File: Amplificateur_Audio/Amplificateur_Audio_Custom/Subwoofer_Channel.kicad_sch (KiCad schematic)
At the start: 52 parts, among them J901 I2S-OUT, J902 RCJ-024, U901 PCM5252RHBR, U902 NE5532

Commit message: Assignation des composants et empreintes terminé
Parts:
- removed C920: 22pF, symbol Device:C_Small
- removed C921, C923: 10uF, symbol Device:C_Small
- removed JP905: DIN2-SEL, symbol Jumper:Jumper_3_Open
- added C915: 10uF, Capacitor_SMD:C_1206_3216Metric_Pad1.33x1.80mm_HandSolder, symbol Device:C_Small
- added C918: 10uF, Capacitor_SMD:C_0603_1608Metric_Pad1.08x0.95mm_HandSolder, symbol Device:C_Small
- added C919: 22pF, Capacitor_SMD:C_0603_1608Metric_Pad1.08x0.95mm_HandSolder, symbol Device:C_Small
- added JP901: DIN2-SEL, Connector_PinHeader_2.54mm:PinHeader_1x03_P2.54mm_Vertical_SMD_Pin1Left, symbol Jumper:Jumper_3_Open
- C901, C902, C905, C910, C912, C914, C917, C922, C924: footprint (none) -> Capacitor_SMD:C_0603_1608Metric_Pad1.08x0.95mm_HandSolder
- C903, C904, C906, C907, C908, C909, C911: footprint (none) -> Capacitor_SMD:C_0402_1005Metric_Pad0.74x0.62mm_HandSolder
- C913: footprint (none) -> Capacitor_SMD:C_1206_3216Metric_Pad1.33x1.80mm_HandSolder
- C916, C925: footprint (none) -> Capacitor_SMD:C_0805_2012Metric_Pad1.18x1.45mm_HandSolder
- J901: footprint (none) -> Connector_IDC:IDC-Header_2x10_P2.54mm_Vertical_SMD
- J902: footprint (none) -> NewLibrary:CUI_RCJ-024
- L901: footprint (none) -> Inductor_SMD:L_APV_ANR4012
- R901, R909, R910, R911, R912, R915: footprint (none) -> Resistor_SMD:R_0603_1608Metric_Pad0.98x0.95mm_HandSolder
- R902, R903, R904, R905, R908, R913, R914, R916, R917, R918, R919, R920, R921, R922: footprint (none) -> Resistor_SMD:R_0402_1005Metric_Pad0.72x0.64mm_HandSolder
- R906: footprint (none) -> Resistor_SMD:R_0402_1005Metric_Pad0.72x0.64mm_HandSolder; now not fitted
- R907: footprint (none) -> Resistor_SMD:R_0402_1005Metric_Pad0.72x0.64mm_HandSolder; now fitted
- U901: footprint (none) -> Package_DFN_QFN:Texas_RHB0032E_VQFN-32-1EP_5x5mm_P0.5mm_EP3.45x3.45mm_ThermalVias
- U902: footprint (none) -> Package_SO:Texas_HTSOP-8-1EP_3.9x4.9mm_P1.27mm_EP2.95x4.9mm_Mask2.4x3.1mm_ThermalVias
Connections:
- net 12V-OA: now also C916.2, R921.2; no longer R922.1
- net 3V3: now also R906.2, R908.2; no longer R906.1, R907.2
- net DIN2: now also JP901.2 (C)
- net GND: now also C908.1, C916.1, R907.1, R922.1, C918.2; no longer C908.2, R908.1, R921.2
- net at C922.1, R921.1, R922.2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: now also R920.1, C918.1, C919.1; no longer R920.2
- net at C917.2, R915.2, U902.1: now also R917.1; no longer R919.1
- net at J901.11 (Pin_11): now also JP901.1 (A)
- net at J901.13 (Pin_13): now also JP901.3 (B)
- net at C917.1, U902.2 (-): now also R917.2, R918.1; no longer R917.1, R919.2
- net at C913.2: now also R918.2; no longer R917.2
- net at C912.1, R910.1, R914.1: now also C915.1; no longer C916.1
- net at U901.2 (LDOO): now also C908.2; no longer C908.1
- net at U901.1 (XSMT): now also R908.1; no longer R906.2
- new net: C915.2, R919.2
- new net: R906.1, R907.2, U901.22 (GPIO2/ADR2/GPO)
- new net: C919.2, R919.1, R920.2, U902.3 (+)

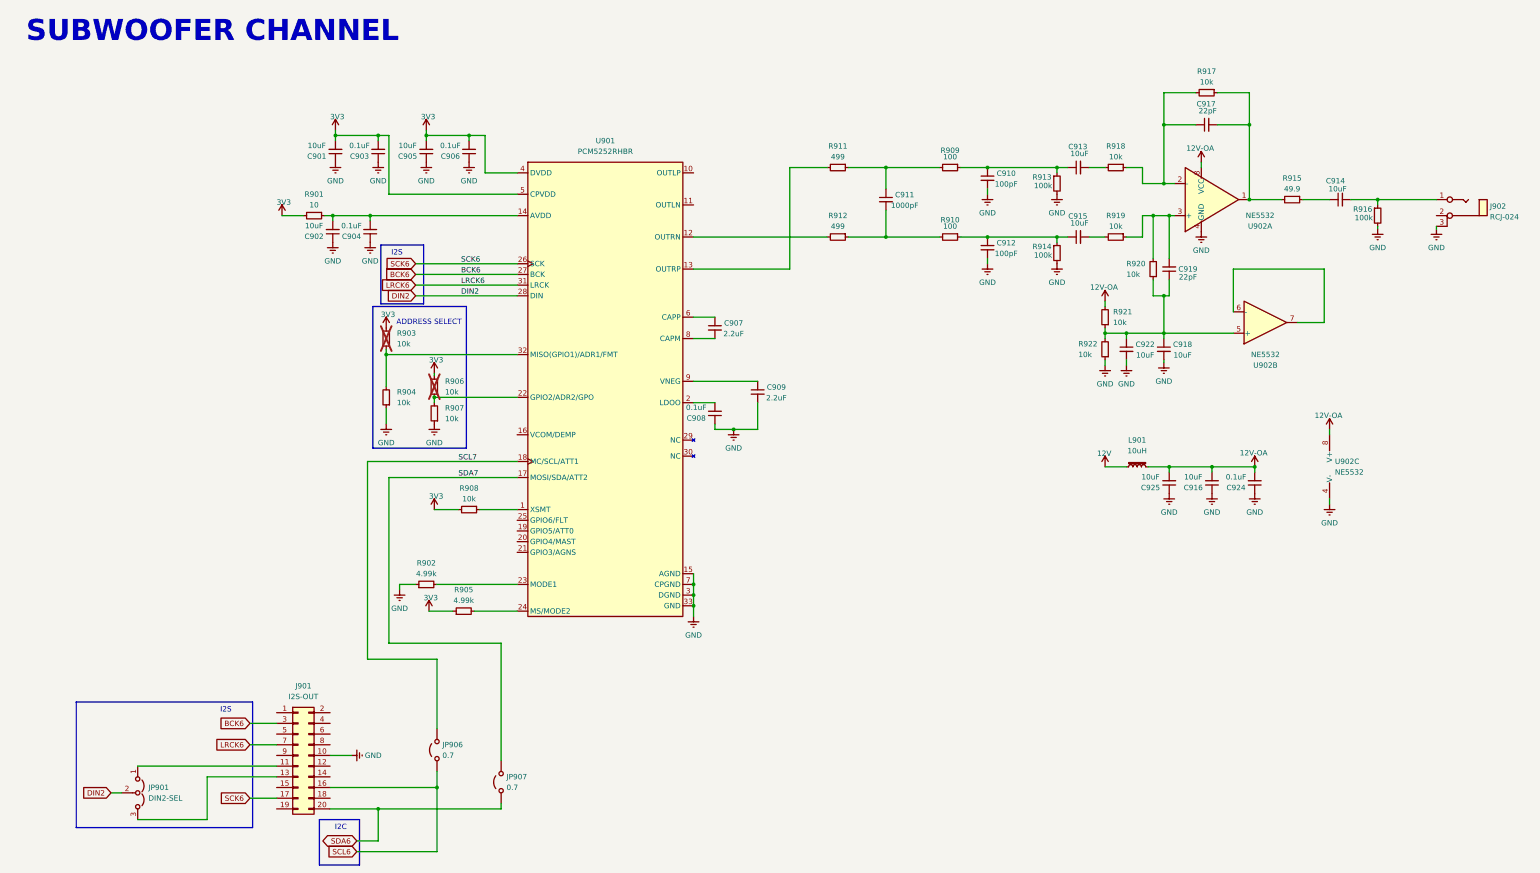
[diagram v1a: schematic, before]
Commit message: Ajout de point de test et début du routage
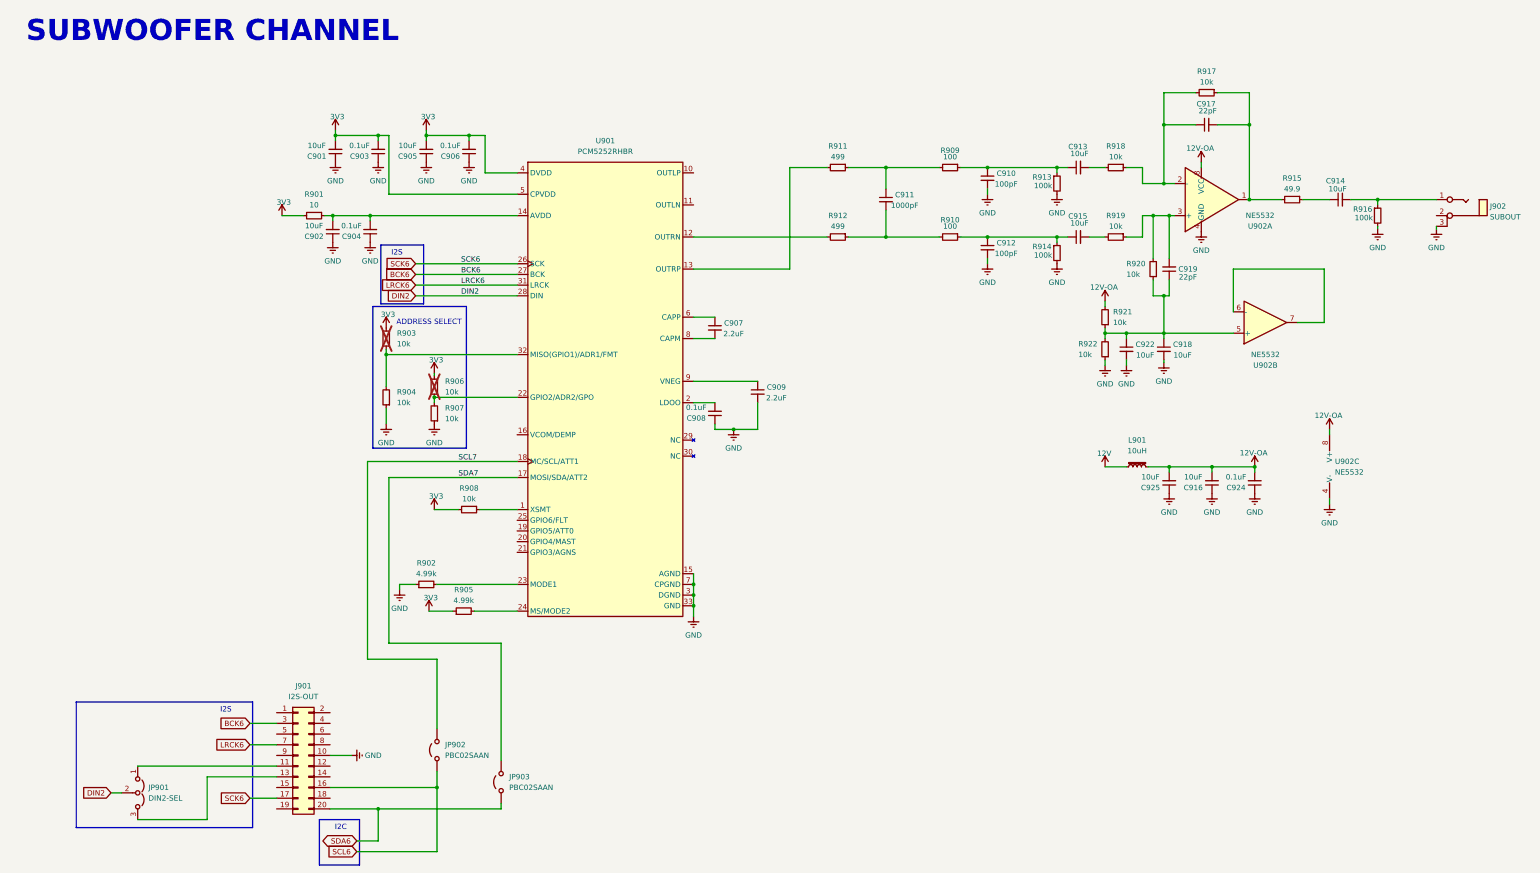
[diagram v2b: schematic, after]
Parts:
- removed JP906, JP907: 0.7, symbol Jumper:Jumper_2_Open
- added JP902, JP903: PBC02SAAN, NewLibrary:PBC02SAAN, symbol Jumper:Jumper_2_Open
- J902: value RCJ-024 -> SUBOUT
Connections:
- net SCL6: now also JP902.1 (A)
- net SCL7: now also JP902.2 (B)
- net SDA6: now also JP903.1 (A)
- net SDA7: now also JP903.2 (B)
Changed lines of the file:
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@@
+	)
+	(symbol
+		(lib_id "Jumper:Jumper_2_Open")
+		(at 129.54 201.93 90)
+		(unit 1)
+		(exclude_from_sim no)
+		(in_bom yes)
+		(on_board yes)
+		(dnp no)
+		(fields_autoplaced yes)
+		(property "Reference" "JP902"
+			(at 131.445 200.6599 90)
+			(effects
+				(font
+					(size 1.27 1.27)
+				)
+				(justify right)
+			)
+		)
+		(property "Value" "PBC02SAAN"
+			(at 131.445 203.1999 90)
+			(effects
+				(font
+					(size 1.27 1.27)
+				)
+				(justify right)
+			)
+		)
+		(property "Footprint" "NewLibrary:PBC02SAAN"
+			(at 129.54 201.93 0)
+			(effects
+				(font
+					(size 1.27 1.27)
+				)
+				(hide yes)
+			)
+		)
+		(property "Datasheet" "~"
+			(at 129.54 201.93 0)
+			(effects
+				(font
+					(size 1.27 1.27)
+				)
+				(hide yes)
+			)
+		)
+		(property "Description" "Jumper, 2-pole, open"
+			(at 129.54 201.93 0)
+			(effects
+				(font
+					(size 1.27 1.27)
+				)
+				(hide yes)
+			)
+		)
+		(pin "2"
+		)
+		(pin "1"
+		)
+		(instances
+			(project "Amplificateur_Audio"
+				(path "/bf9cc67f-178f-4c8c-b6a6-249a1896d599/c3eeb04c-3089-42ef-a9c1-68f6f54d6f1b"
+					(reference "JP902")
+					(unit 1)
+				)
+			)
+		)
 	)
 	(symbol
@@
 	)
 	(symbol
+		(lib_id "Jumper:Jumper_2_Open")
+		(at 144.78 209.55 90)
+		(unit 1)
+		(exclude_from_sim no)
+		(in_bom yes)
+		(on_board yes)
+		(dnp no)
+		(fields_autoplaced yes)
+		(property "Reference" "JP903"
+			(at 146.685 208.2799 90)
+			(effects
+				(font
+					(size 1.27 1.27)
+				)
+				(justify right)
+			)
+		)
+		(property "Value" "PBC02SAAN"
+			(at 146.685 210.8199 90)
+			(effects
+				(font
+					(size 1.27 1.27)
+				)
+				(justify right)
+			)
+		)
+		(property "Footprint" "NewLibrary:PBC02SAAN"
+			(at 144.78 209.55 0)
+			(effects
+				(font
+					(size 1.27 1.27)
+				)
+				(hide yes)
+			)
+		)
+		(property "Datasheet" "~"
+			(at 144.78 209.55 0)
+			(effects
+				(font
+					(size 1.27 1.27)
+				)
+				(hide yes)
+			)
+		)
+		(property "Description" "Jumper, 2-pole, open"
+			(at 144.78 209.55 0)
+			(effects
+				(font
+					(size 1.27 1.27)
+				)
+				(hide yes)
+			)
+		)
+		(pin "2"
+		)
+		(pin "1"
+		)
+		(instances
+			(project "Amplificateur_Audio"
+				(path "/bf9cc67f-178f-4c8c-b6a6-249a1896d599/c3eeb04c-3089-42ef-a9c1-68f6f54d6f1b"
+					(reference "JP903")
+					(unit 1)
+				)
+			)
+		)
+	)
+	(symbol
 		(lib_id "power:Earth")
 		(at 105.41 62.23 0)
@@
 	)
 	(symbol
-		(lib_id "Jumper:Jumper_2_Open")
-		(at 144.78 209.55 90)
-		(unit 1)
-		(exclude_from_sim no)
-		(in_bom yes)
-		(on_board yes)
-		(dnp no)
-		(fields_autoplaced yes)
-		(property "Reference" "JP907"
-			(at 146.05 208.2799 90)
-			(effects
-				(font
-					(size 1.27 1.27)
-				)
-				(justify right)
-			)
-		)
-		(property "Value" "0.7"
-			(at 146.05 210.8199 90)
-			(effects
-				(font
-					(size 1.27 1.27)
-				)
-				(justify right)
-			)
-		)
-		(property "Footprint" ""
-			(at 144.78 209.55 0)
-			(effects
-				(font
-					(size 1.27 1.27)
-				)
-				(hide yes)
-			)
-		)
-		(property "Datasheet" "~"
-			(at 144.78 209.55 0)
-			(effects
-				(font
-					(size 1.27 1.27)
-				)
-				(hide yes)
-			)
-		)
-		(property "Description" "Jumper, 2-pole, open"
-			(at 144.78 209.55 0)
-			(effects
-				(font
-					(size 1.27 1.27)
-				)
-				(hide yes)
-			)
-		)
-		(pin "2"
-		)
-		(pin "1"
-		)
-		(instances
-			(project "BarreDeSonTI"
-				(path "/bf9cc67f-178f-4c8c-b6a6-249a1896d599/c3eeb04c-3089-42ef-a9c1-68f6f54d6f1b"
-					(reference "JP907")
-					(unit 1)
-				)
-			)
-		)
-	)
-	(symbol
 		(lib_id "power:Earth")
 		(at 104.775 81.28 0)
@@
 			)
 		)
-		(property "Value" "RCJ-024"
+		(property "Value" "SUBOUT"
 			(at 379.73 75.2474 0)
 			(effects
@@
 					(unit 1)
 				)
-			)
-		)
-	)
-	(symbol
-		(lib_id "Jumper:Jumper_2_Open")
-		(at 129.54 201.93 90)
-		(unit 1)
-		(exclude_from_sim no)
-		(in_bom yes)
-		(on_board yes)
-		(dnp no)
-		(fields_autoplaced yes)
-		(property "Reference" "JP906"
-			(at 130.81 200.6599 90)
-			(effects
-				(font
-					(size 1.27 1.27)
-				)
-				(justify right)
-			)
-		)
-		(property "Value" "0.7"
-			(at 130.81 203.1999 90)
-			(effects
-				(font
-					(size 1.27 1.27)
-				)
-				(justify right)
-			)
-		)
-		(property "Footprint" ""
-			(at 129.54 201.93 0)
-			(effects
-				(font
-					(size 1.27 1.27)
-				)
-				(hide yes)
-			)
-		)
-		(property "Datasheet" "~"
-			(at 129.54 201.93 0)
-			(effects
-				(font
-					(size 1.27 1.27)
-				)
-				(hide yes)
-			)
-		)
-		(property "Description" "Jumper, 2-pole, open"
-			(at 129.54 201.93 0)
-			(effects
-				(font
-					(size 1.27 1.27)
-				)
-				(hide yes)
-			)
-		)
-		(pin "2"
-		)
-		(pin "1"
-		)
-		(instances
-			(project "BarreDeSonTI"
-				(path "/bf9cc67f-178f-4c8c-b6a6-249a1896d599/c3eeb04c-3089-42ef-a9c1-68f6f54d6f1b"
-					(reference "JP906")
-					(unit 1)
-				)

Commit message: Refactor : hierarchical template channels for multichannel routing
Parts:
- C901, C902, C905, C910, C912, C914, C917, C918, C919, C922, C924: footprint Capacitor_SMD:C_0603_1608Metric_Pad1.08x0.95mm_HandSolder -> Capacitor_SMD:C_0603_1608Metric
- C903, C904, C906, C907, C908, C909, C911: footprint Capacitor_SMD:C_0402_1005Metric_Pad0.74x0.62mm_HandSolder -> Capacitor_SMD:C_0402_1005Metric
- C913, C915: footprint Capacitor_SMD:C_1206_3216Metric_Pad1.33x1.80mm_HandSolder -> Capacitor_SMD:C_1206_3216Metric
- C916, C925: footprint Capacitor_SMD:C_0805_2012Metric_Pad1.18x1.45mm_HandSolder -> Capacitor_SMD:C_0805_2012Metric
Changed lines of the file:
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@@
 			)
 		)
-		(property "Footprint" "Capacitor_SMD:C_0603_1608Metric_Pad1.08x0.95mm_HandSolder"
+		(property "Footprint" "Capacitor_SMD:C_0603_1608Metric"
 			(at 344.17 71.12 0)
 			(effects
@@
 			)
 		)
-		(property "Footprint" "Capacitor_SMD:C_1206_3216Metric_Pad1.33x1.80mm_HandSolder"
+		(property "Footprint" "Capacitor_SMD:C_1206_3216Metric"
 			(at 281.94 80.01 0)
 			(effects
@@
 			)
 		)
-		(property "Footprint" "Capacitor_SMD:C_0603_1608Metric_Pad1.08x0.95mm_HandSolder"
+		(property "Footprint" "Capacitor_SMD:C_0603_1608Metric"
 			(at 323.85 138.43 0)
 			(effects
@@
 			)
 		)
-		(property "Footprint" "Capacitor_SMD:C_0603_1608Metric_Pad1.08x0.95mm_HandSolder"
+		(property "Footprint" "Capacitor_SMD:C_0603_1608Metric"
 			(at 302.26 106.68 0)
 			(effects
@@
 			)
 		)
-		(property "Footprint" "Capacitor_SMD:C_0603_1608Metric_Pad1.08x0.95mm_HandSolder"
+		(property "Footprint" "Capacitor_SMD:C_0603_1608Metric"
 			(at 105.41 59.69 0)
 			(effects
@@
 			)
 		)
-		(property "Footprint" "Capacitor_SMD:C_0603_1608Metric_Pad1.08x0.95mm_HandSolder"
+		(property "Footprint" "Capacitor_SMD:C_0603_1608Metric"
 			(at 104.775 78.74 0)
 			(effects
@@
 			)
 		)
-		(property "Footprint" "Capacitor_SMD:C_0402_1005Metric_Pad0.74x0.62mm_HandSolder"
+		(property "Footprint" "Capacitor_SMD:C_0402_1005Metric"
 			(at 195.58 101.6 0)
 			(effects
@@
 			)
 		)
-		(property "Footprint" "Capacitor_SMD:C_0805_2012Metric_Pad1.18x1.45mm_HandSolder"
+		(property "Footprint" "Capacitor_SMD:C_0805_2012Metric"
 			(at 303.53 138.43 0)
 			(effects
@@
 			)
 		)
-		(property "Footprint" "Capacitor_SMD:C_0402_1005Metric_Pad0.74x0.62mm_HandSolder"
+		(property "Footprint" "Capacitor_SMD:C_0402_1005Metric"
 			(at 205.74 116.84 0)
 			(effects
@@
 			)
 		)
-		(property "Footprint" "Capacitor_SMD:C_0603_1608Metric_Pad1.08x0.95mm_HandSolder"
+		(property "Footprint" "Capacitor_SMD:C_0603_1608Metric"
 			(at 260.35 82.55 0)
 			(effects
@@
 			)
 		)
-		(property "Footprint" "Capacitor_SMD:C_0603_1608Metric_Pad1.08x0.95mm_HandSolder"
+		(property "Footprint" "Capacitor_SMD:C_0603_1608Metric"
 			(at 312.42 53.34 0)
 			(effects
@@
 			)
 		)
-		(property "Footprint" "Capacitor_SMD:C_1206_3216Metric_Pad1.33x1.80mm_HandSolder"
+		(property "Footprint" "Capacitor_SMD:C_1206_3216Metric"
 			(at 281.94 63.5 0)
 			(effects
@@
 			)
 		)
-		(property "Footprint" "Capacitor_SMD:C_0805_2012Metric_Pad1.18x1.45mm_HandSolder"
+		(property "Footprint" "Capacitor_SMD:C_0805_2012Metric"
 			(at 313.69 138.43 0)
 			(effects
@@
 			)
 		)
-		(property "Footprint" "Capacitor_SMD:C_0603_1608Metric_Pad1.08x0.95mm_HandSolder"
+		(property "Footprint" "Capacitor_SMD:C_0603_1608Metric"
 			(at 293.37 106.68 0)
 			(effects
@@
 			)
 		)
-		(property "Footprint" "Capacitor_SMD:C_0402_1005Metric_Pad0.74x0.62mm_HandSolder"
+		(property "Footprint" "Capacitor_SMD:C_0402_1005Metric"
 			(at 195.58 121.92 0)
 			(effects
@@
 			)
 		)
-		(property "Footprint" "Capacitor_SMD:C_0402_1005Metric_Pad0.74x0.62mm_HandSolder"
+		(property "Footprint" "Capacitor_SMD:C_0402_1005Metric"
 			(at 236.22 71.12 0)
 			(effects
@@
 			)
 		)
-		(property "Footprint" "Capacitor_SMD:C_0603_1608Metric_Pad1.08x0.95mm_HandSolder"
+		(property "Footprint" "Capacitor_SMD:C_0603_1608Metric"
 			(at 260.35 66.04 0)
 			(effects
@@
 			)
 		)
-		(property "Footprint" "Capacitor_SMD:C_0603_1608Metric_Pad1.08x0.95mm_HandSolder"
+		(property "Footprint" "Capacitor_SMD:C_0603_1608Metric"
 			(at 127 59.69 0)
 			(effects
@@
 			)
 		)
-		(property "Footprint" "Capacitor_SMD:C_0402_1005Metric_Pad0.74x0.62mm_HandSolder"
+		(property "Footprint" "Capacitor_SMD:C_0402_1005Metric"
 			(at 115.57 59.69 0)
 			(effects
@@
 			)
 		)
-		(property "Footprint" "Capacitor_SMD:C_0402_1005Metric_Pad0.74x0.62mm_HandSolder"
+		(property "Footprint" "Capacitor_SMD:C_0402_1005Metric"
 			(at 137.16 59.69 0)
 			(effects
@@
 			)
 		)
-		(property "Footprint" "Capacitor_SMD:C_0603_1608Metric_Pad1.08x0.95mm_HandSolder"
+		(property "Footprint" "Capacitor_SMD:C_0603_1608Metric"
 			(at 303.53 87.63 0)
 			(effects
@@
 			)
 		)
-		(property "Footprint" "Capacitor_SMD:C_0402_1005Metric_Pad0.74x0.62mm_HandSolder"
+		(property "Footprint" "Capacitor_SMD:C_0402_1005Metric"
 			(at 113.665 78.74 0)
 			(effects
